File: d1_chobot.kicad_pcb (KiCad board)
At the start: 2 copper layers, 59.7 x 33.7 mm, 23 parts, among them J1 LDR HW, J2 LDR CH, J3 PWM HW, J4 PWM CH, Q1 2N7000, Q2 2N7000, U1 LM393, U2 WeMos_D1_mini

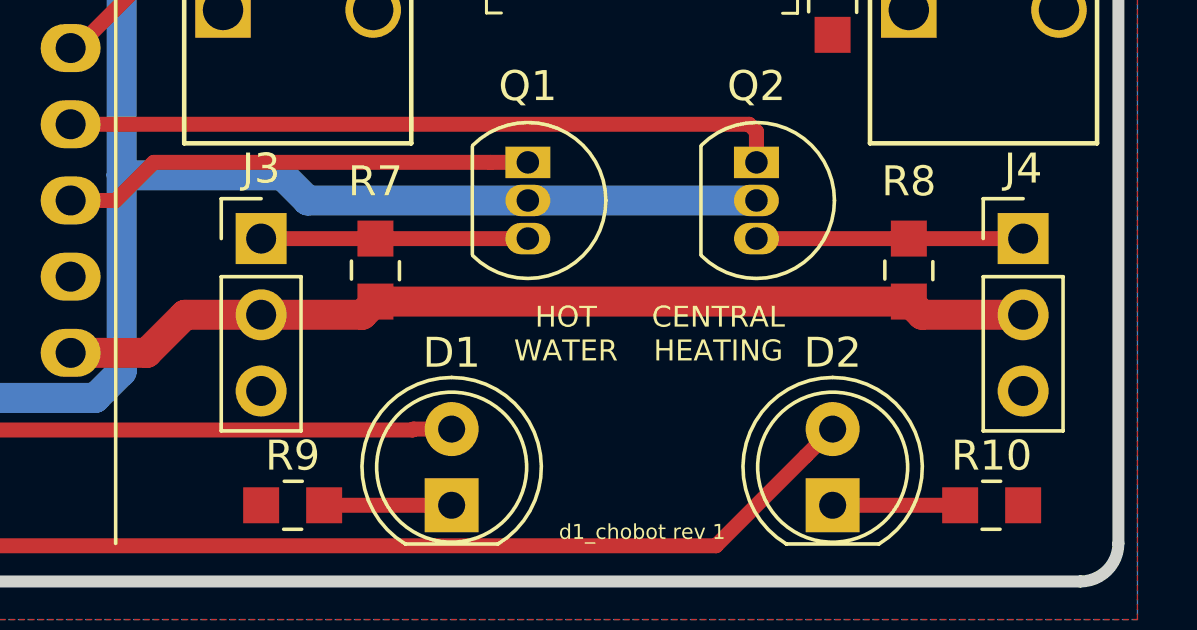
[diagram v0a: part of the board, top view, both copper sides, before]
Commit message: Add ORB to PWM jumpers.
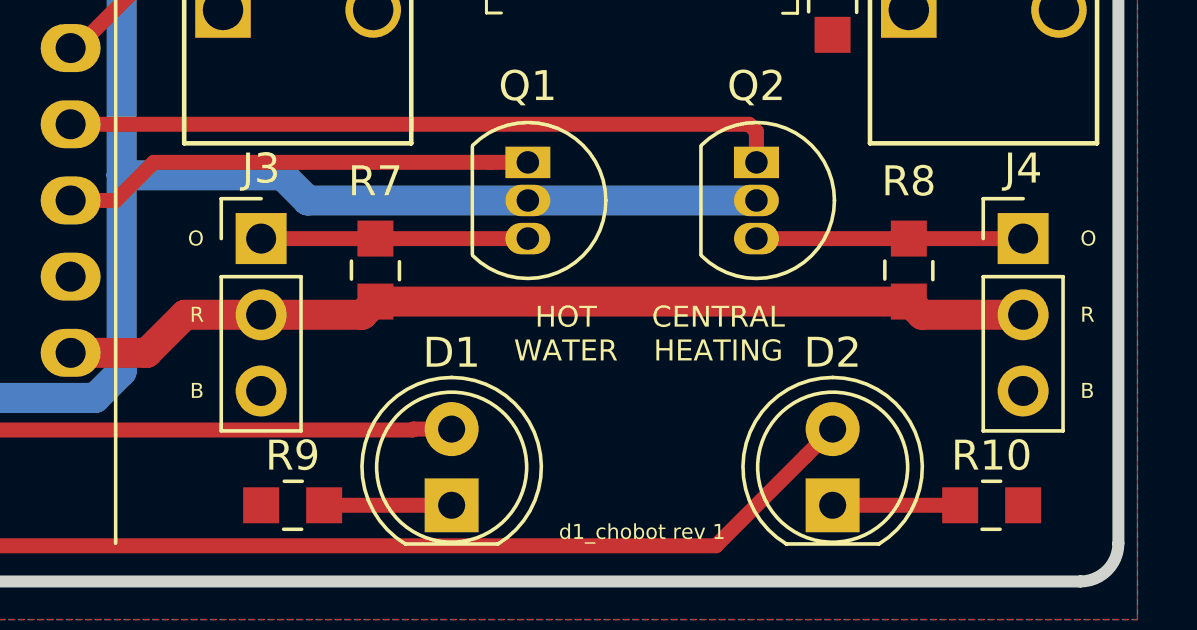
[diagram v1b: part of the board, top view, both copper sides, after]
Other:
- board text added: "B"
- board text added: "O"
- board text added: "R"
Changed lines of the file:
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@@
   (general
     (thickness 1.6)
-    (drawings 16)
+    (drawings 22)
     (tracks 93)
     (zones 0)
@@
       (net 15 LDR_HW))
   )
+  (gr_text R (at 197.485 97.79) (layer F.SilkS)
+    (effects (font (size 0.5 0.5) (thickness 0.125)) (justify left))
+  )
+  (gr_text B (at 197.485 100.33) (layer F.SilkS)
+    (effects (font (size 0.5 0.5) (thickness 0.125)) (justify left))
+  )
+  (gr_text O (at 197.485 95.25) (layer F.SilkS)
+    (effects (font (size 0.5 0.5) (thickness 0.125)) (justify left))
+  )
+  (gr_text B (at 168.275 100.33) (layer F.SilkS)
+    (effects (font (size 0.5 0.5) (thickness 0.125)) (justify right))
+  )
+  (gr_text R (at 168.275 97.79) (layer F.SilkS)
+    (effects (font (size 0.5 0.5) (thickness 0.125)) (justify right))
+  )
+  (gr_text O (at 168.275 95.25) (layer F.SilkS)
+    (effects (font (size 0.5 0.5) (thickness 0.125)) (justify right))
+  )
   (gr_text "d1_chobot rev 1" (at 182.88 105.029) (layer F.SilkS)
